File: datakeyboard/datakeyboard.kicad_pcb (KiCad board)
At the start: 2 copper layers, 57.3 x 41.2 mm, 48 parts, among them Q1 BSS83P, Q2 BSS83P, Q3 BSS83P, Q4 BSS83P, Q5 BSS83P, SW1 SW_Push, SW2 SW_Push, SW3 SW_Push, SW4 SW_Push, SW5 SW_Push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

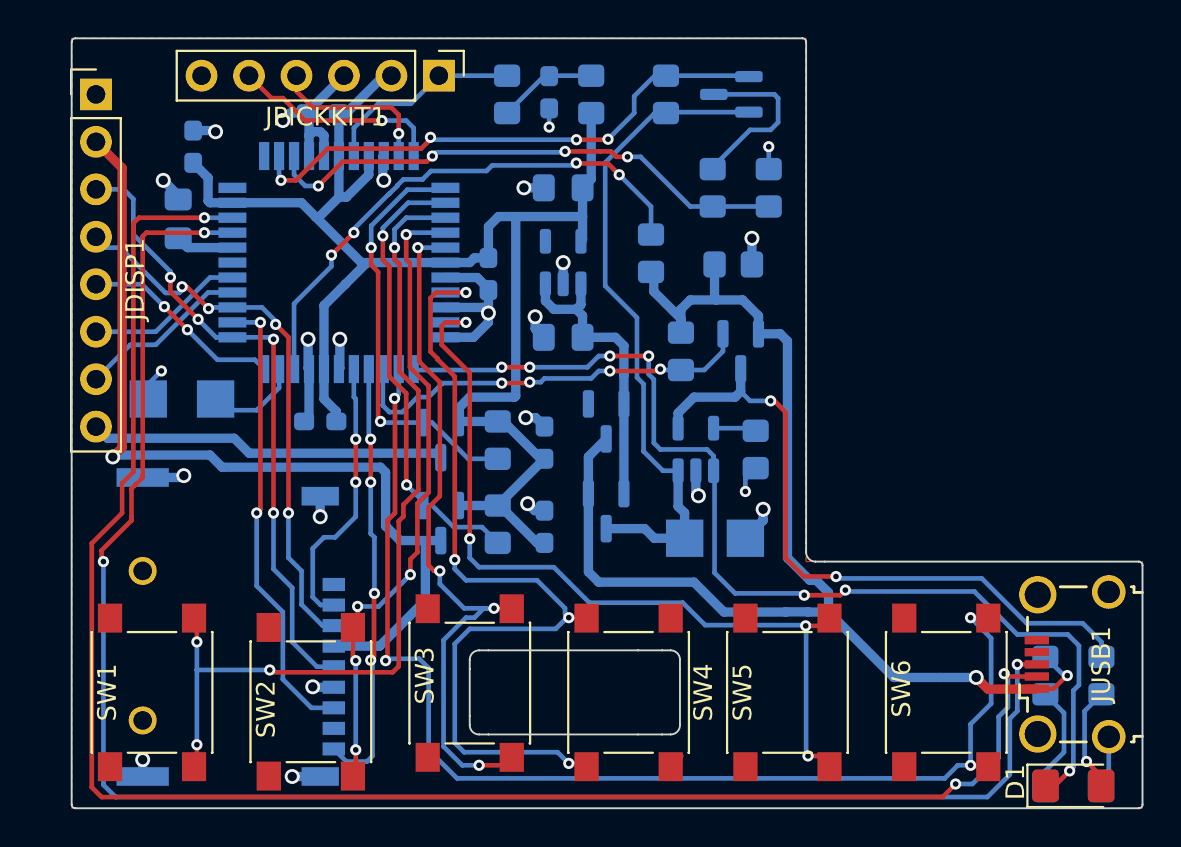
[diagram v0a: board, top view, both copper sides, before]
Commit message: Fix display orientation Switch VBAT, GND text on silk screen Movie VIAs out of the way of the button solder pads.
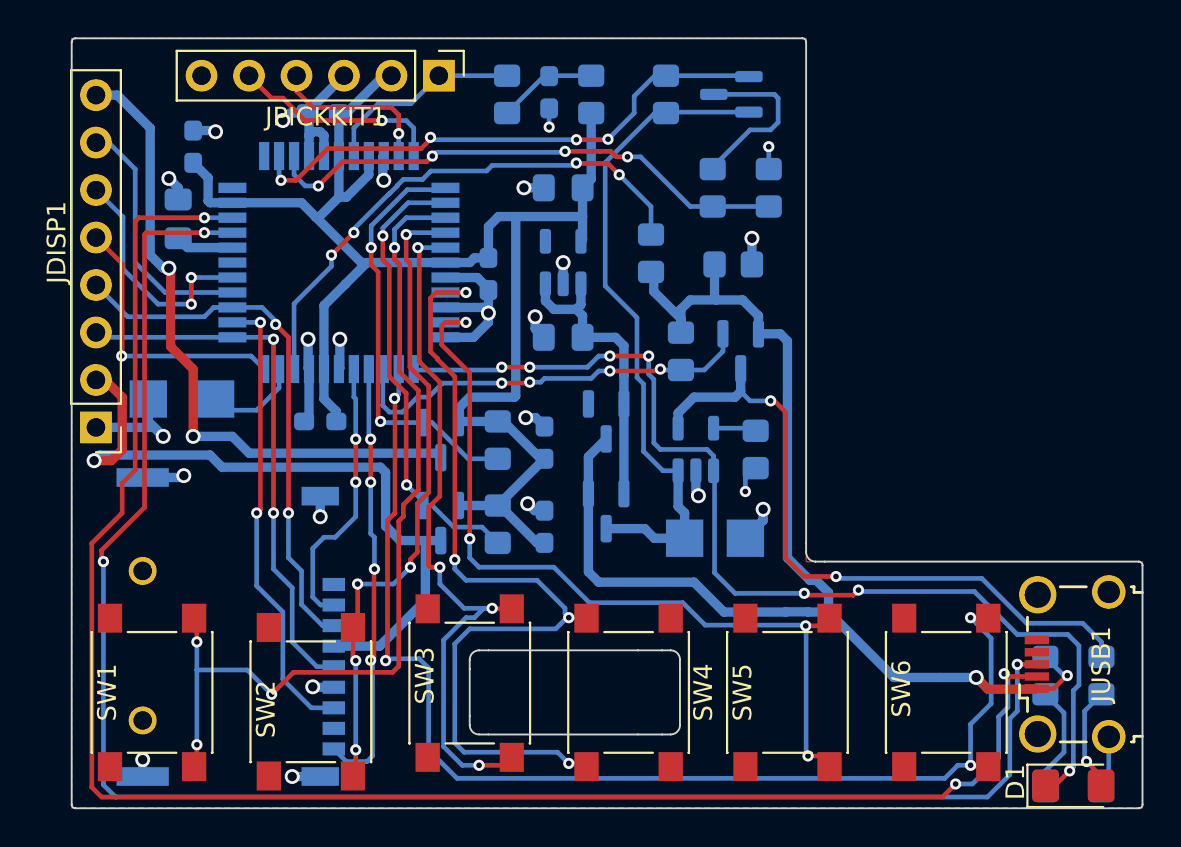
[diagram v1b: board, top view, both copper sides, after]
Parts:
- moved JDISP1 17.8 mm to (102.0, 125.8), turned to 180 degrees
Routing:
- net /LEDA: track 19.1 -> 35.0 mm, vias 0 -> 2
- net /VPER: track 47.9 -> 37.7 mm
- net /SCLK: track 34.0 -> 29.0 mm, vias 4 -> 2
- net /RS_D: track 8.50 -> 12.9 mm, vias 0 -> 2
- net /CS_D: track 9.22 -> 13.6 mm
- net /RES_D: track 10.9 -> 14.8 mm, vias 2 -> 1
- net GND: track 55.1 -> 58.6 mm
- net /MOSI: track 29.9 -> 28.8 mm, vias 4 -> 2
- net /BTN1: track 46.4 -> 47.4 mm

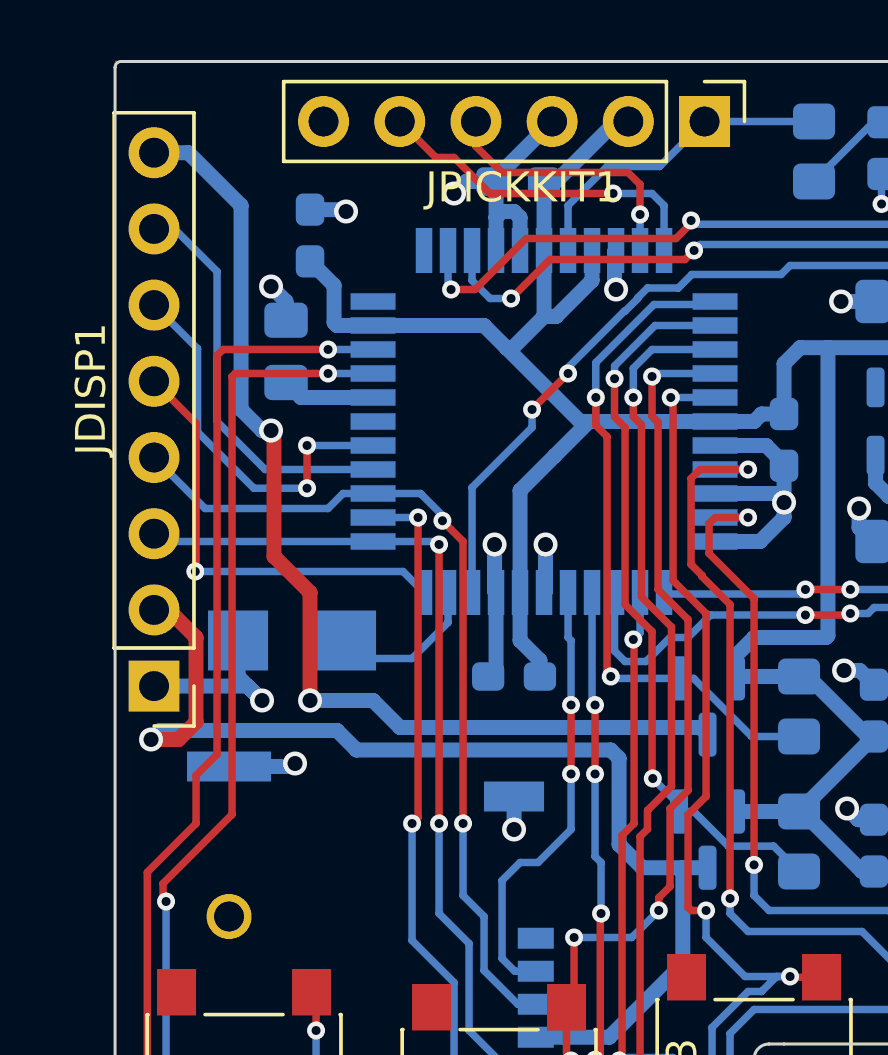
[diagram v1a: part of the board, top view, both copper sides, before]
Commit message: Reduce current to increase battery life
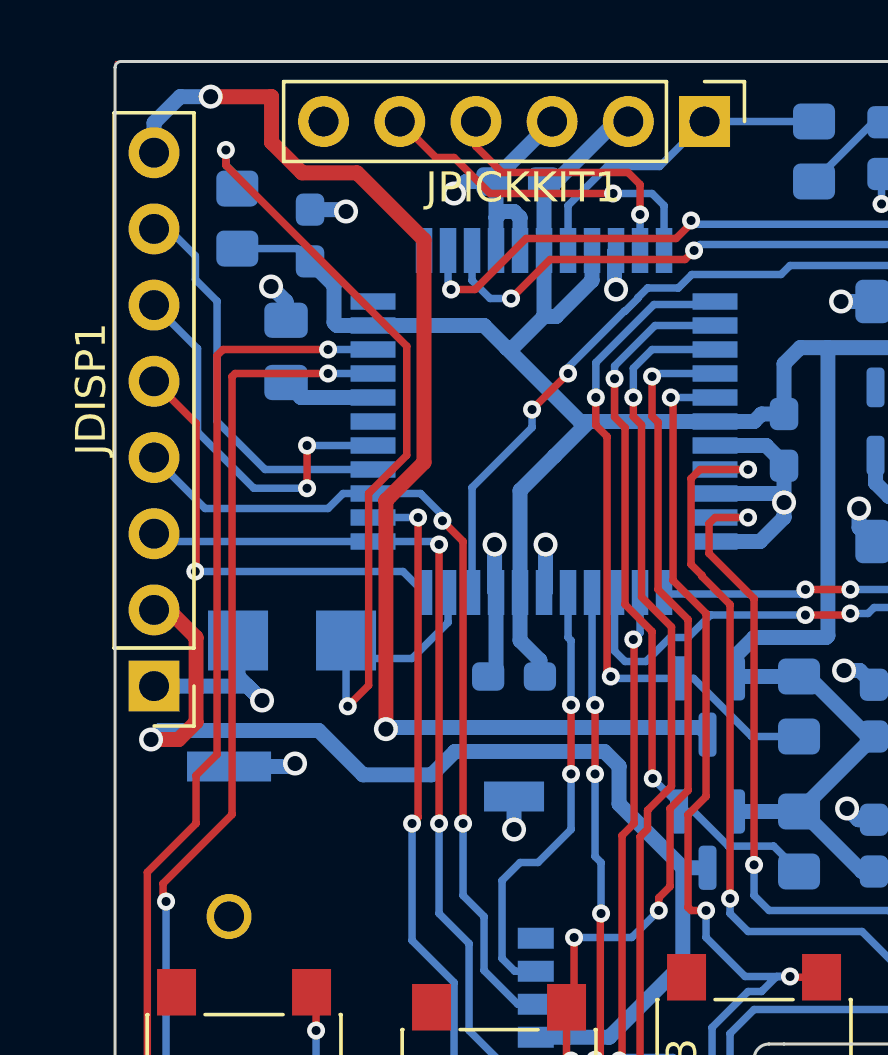
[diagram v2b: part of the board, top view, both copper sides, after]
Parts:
- added R14: 100k, Resistor_SMD:R_0805_2012Metric_Pad1.20x1.40mm_HandSolder, B.Cu at (104.8, 110.2)
- Q1, Q2, Q3, Q4, Q5: value BSS83P -> NX2301P
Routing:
- net /CASE: track 5.15 -> 30.7 mm, vias 0 -> 2
- net /LEDA: track 35.0 -> 40.9 mm
- net +3V0: track 83.6 -> 86.2 mm
